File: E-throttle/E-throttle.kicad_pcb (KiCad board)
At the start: 2 copper layers, 100 x 100 mm, 62 parts, among them IC1 BTS441TG, J3 Conn_01x11, J4 Conn_01x11, J5 776087-1, J9 Micro_SD_Card, Q1 NMOS, SW1 SW_Push, U1 74HC123, U2 LM317_SOT-223, U3 LM317_SOT-223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

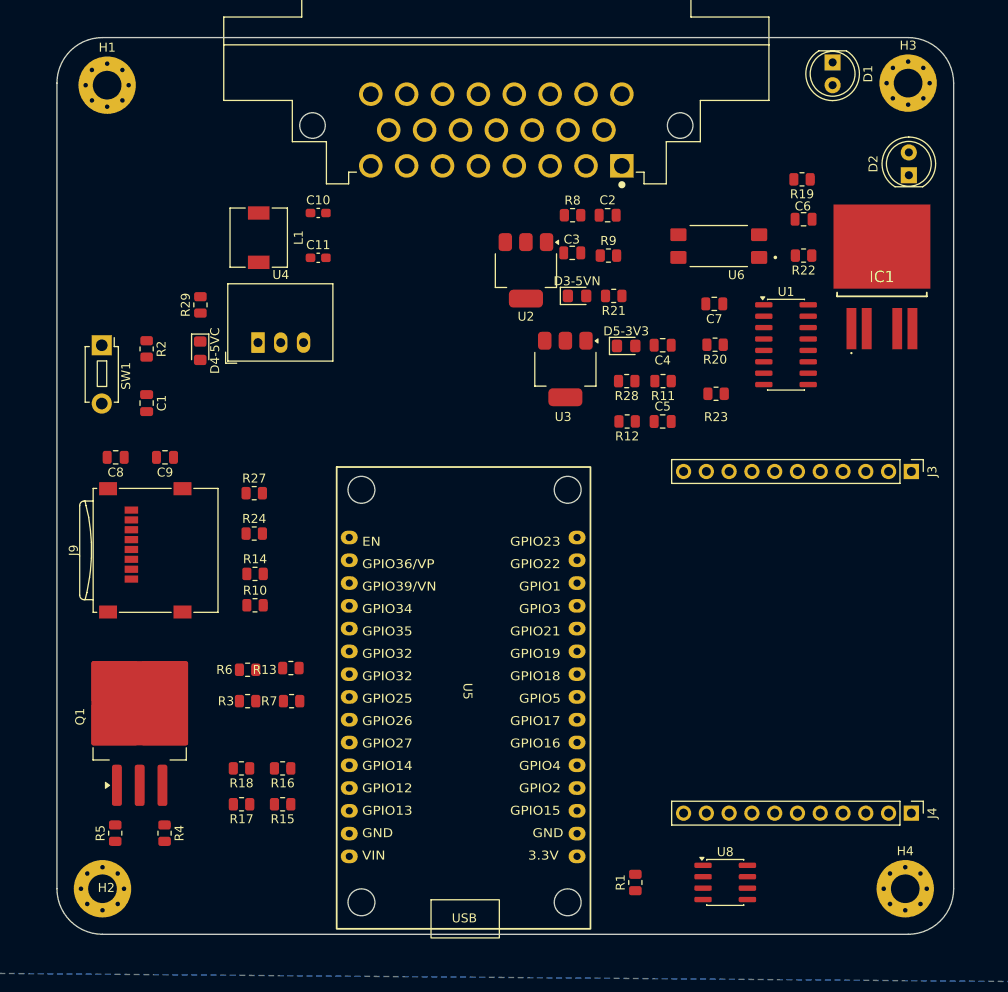
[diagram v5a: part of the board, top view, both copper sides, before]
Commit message: Added majority of routing to PCB layout
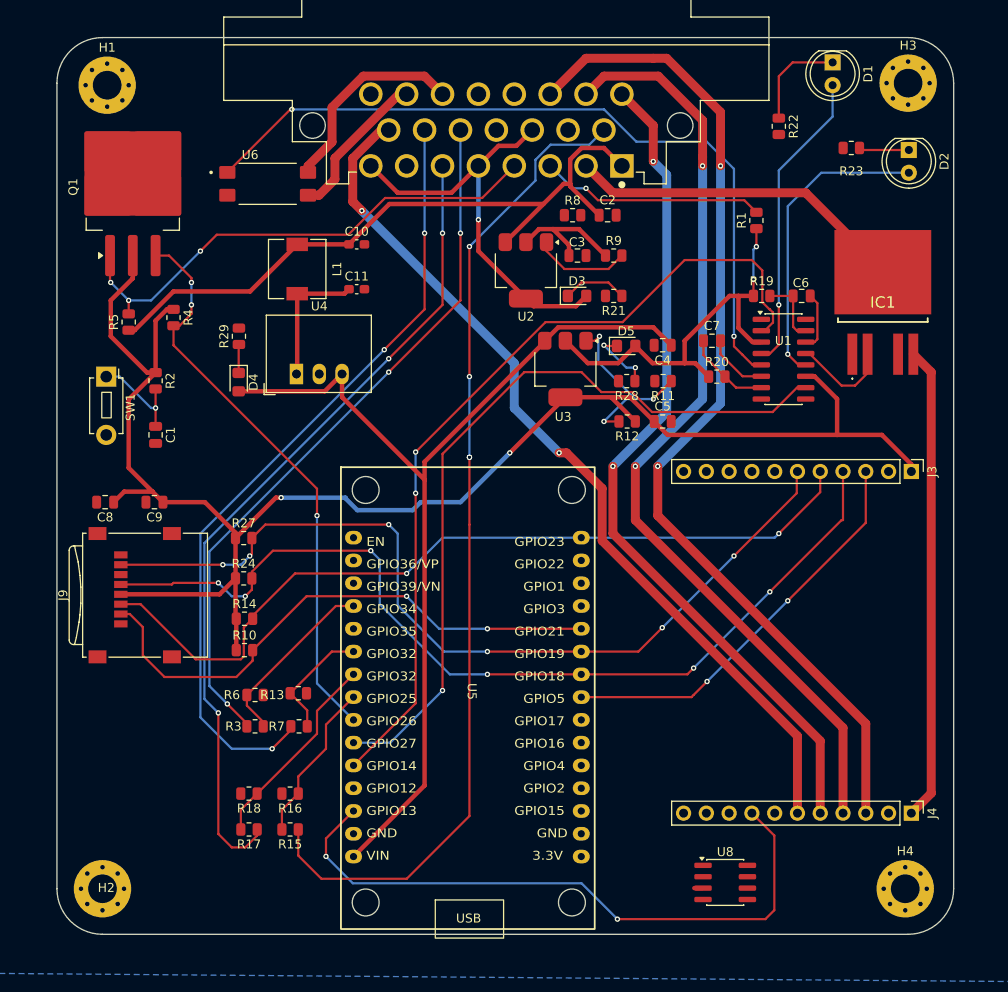
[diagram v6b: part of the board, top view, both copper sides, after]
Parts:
- moved R1 75.0 mm to (232.7, 53.9)
- moved Q1 59.1 mm to (163.2, 50.2)
- moved R4 57.5 mm to (167.7, 64.7)
- moved R5 57.0 mm to (162.7, 65.2)
- moved U6 50.8 mm to (178.2, 49.8), turned to 0 degrees
- moved R23 31.3 mm to (243.3, 45.8)
- moved R22 14.7 mm to (235.2, 43.4), turned to -90 degrees
- moved R19 13.8 mm to (233.3, 62.3), turned to 0 degrees
- moved C6 8.55 mm to (237.8, 62.3)
- moved C10 5.54 mm to (188.2, 56.6)
- moved C11 5.54 mm to (188.2, 61.6)
- moved D4 5.54 mm to (175.0, 71.9)
- moved U4 5.54 mm to (181.4, 71.0)
- moved L1 5.54 mm to (181.5, 59.3)
- moved R29 5.54 mm to (175.0, 66.8)
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- renumbered D3-5VN to D3, D4-5VC to D4, D5-3V3 to D5
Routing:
- net +3V3: track 0.00 -> 229.4 mm, vias 0 -> 4
- net /STEP-2-: track 0.00 -> 113.8 mm, vias 0 -> 2
- net /TPS-SIG2: track 0.00 -> 111.2 mm, vias 0 -> 4
- net +5V: track 0.00 -> 110.1 mm
- net /STEP-2+: track 0.00 -> 105.8 mm, vias 0 -> 2
- net /SPI-SCK: track 0.00 -> 105.7 mm, vias 0 -> 6
- net /STEP-1+: track 0.00 -> 99.4 mm, vias 0 -> 2
- net /SPI-MISO: track 0.00 -> 98.6 mm, vias 0 -> 6
- net /STEP-1-: track 0.00 -> 94.3 mm, vias 0 -> 2
- net /ESP_HEARTBEAT_L1: track 0.00 -> 93.9 mm, vias 0 -> 2
- net /SPI-MOSI: track 0.00 -> 92.6 mm, vias 0 -> 2
- net /TPS-SIG1: track 0.00 -> 92.3 mm, vias 0 -> 3
- net /APPS-SIG2: track 0.00 -> 88.7 mm, vias 0 -> 3
- net /ESP_HEARTBEAT_L2: track 0.00 -> 86.0 mm, vias 0 -> 1
- net /WD_ENABLE_STEP_RELAY: track 0.00 -> 85.9 mm, vias 0 -> 2
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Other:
- board text added: "GPIO19"

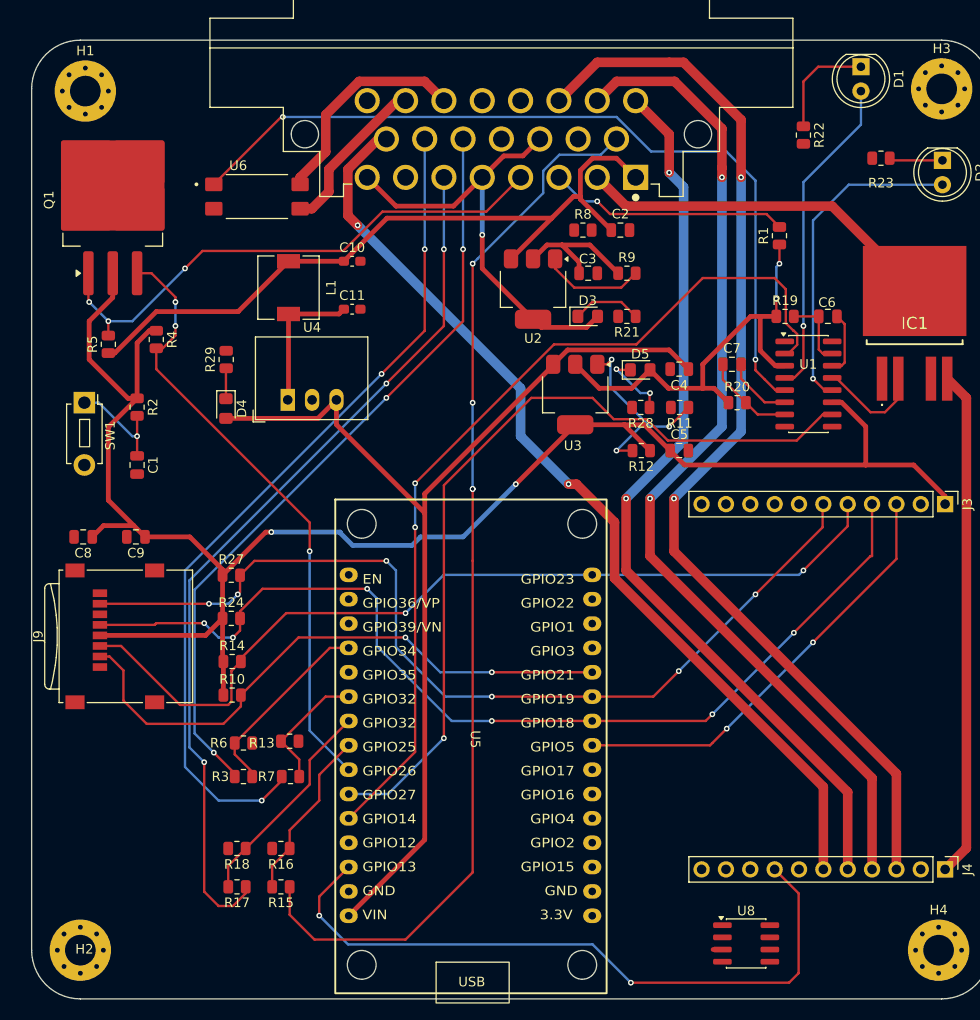
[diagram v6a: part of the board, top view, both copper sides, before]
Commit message: added a few ground vias
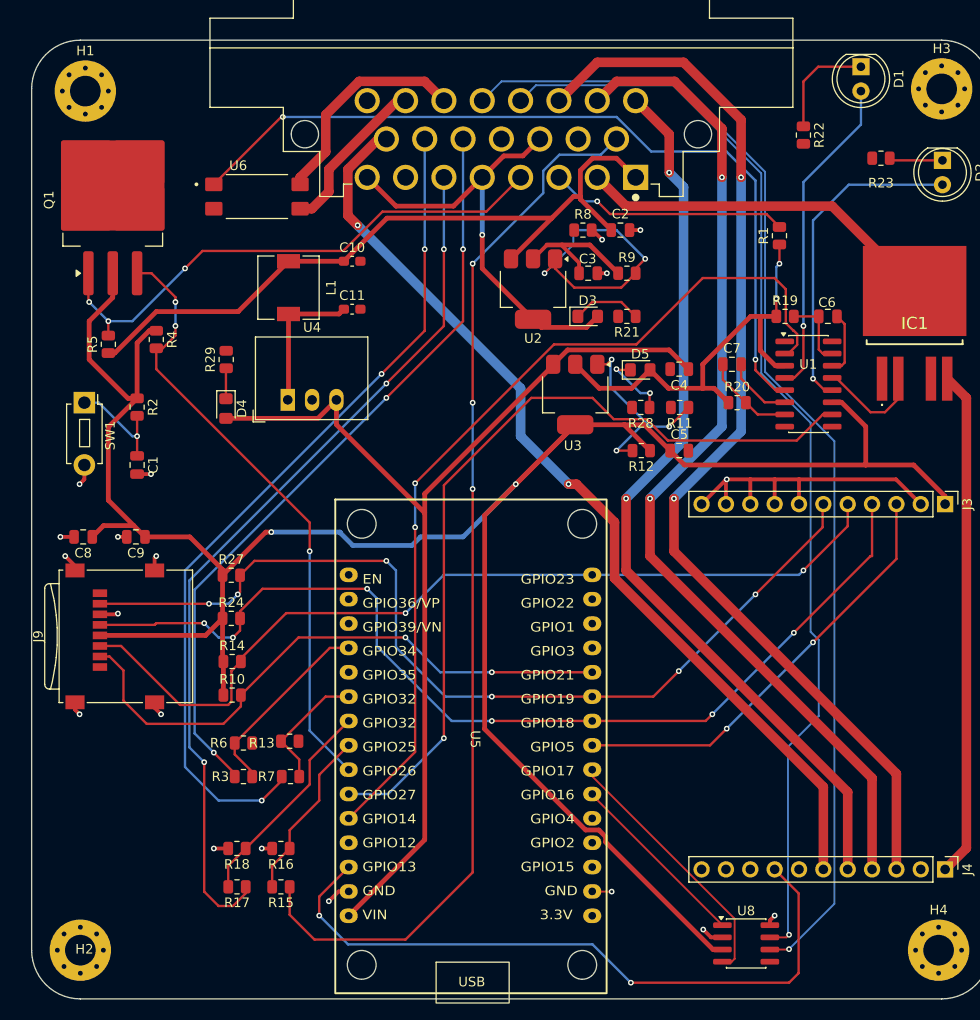
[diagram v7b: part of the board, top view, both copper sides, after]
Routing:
- net /CAN-L: track 0.00 -> 122.3 mm, vias 0 -> 1
- net /CAN-H: track 0.00 -> 115.0 mm, vias 0 -> 1
- net +3V3: track 229.4 -> 298.8 mm
- net GND: track 0.00 -> 61.9 mm, vias 0 -> 18
- net /CAN-RX: track 0.00 -> 27.3 mm
- net /CAN-TX: track 0.00 -> 19.3 mm
- net Net-(U2-ADJ): track 10.8 -> 29.2 mm, vias 0 -> 2
- net unconnected-(U5-GND-Pad17): track 0.00 -> 2.04 mm, vias 0 -> 1
- net +5V-SENSORS: track 61.1 -> 62.6 mm
- net /TPS-SIG2: vias 4 -> 3

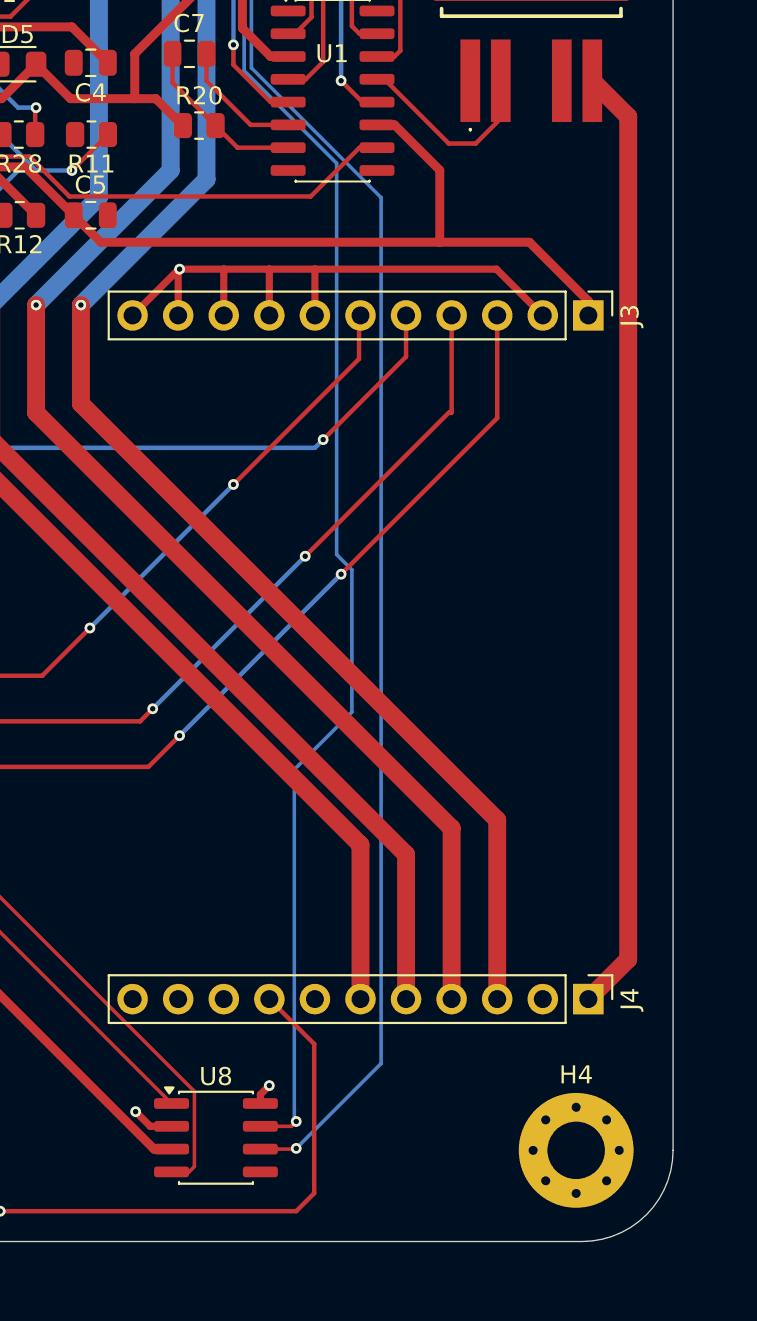
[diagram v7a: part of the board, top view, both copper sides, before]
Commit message: Fix Stepper Driver Spacing
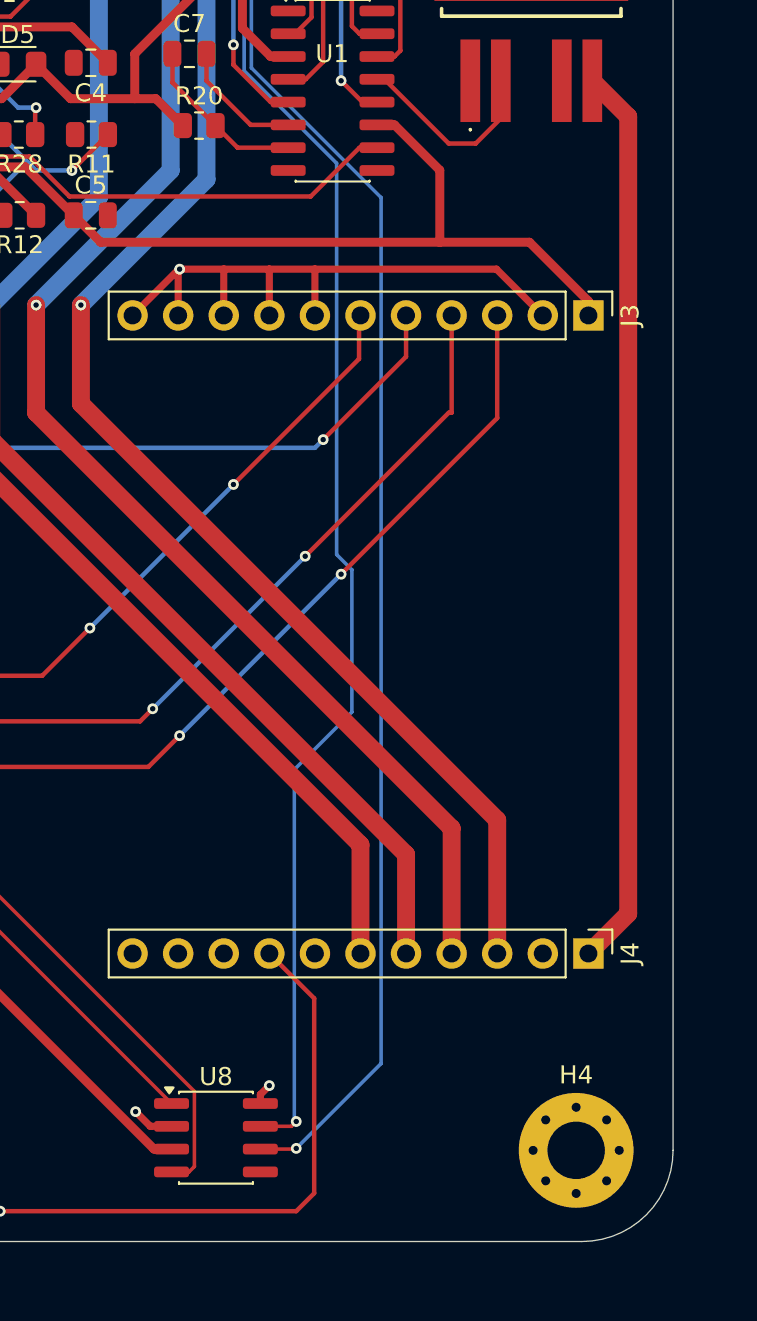
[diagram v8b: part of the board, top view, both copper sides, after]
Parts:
- moved J4 2.54 mm to (250.0, 117.5)
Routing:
- net /DIAG0: track 71.5 -> 74.0 mm
- net /STEP-2-: track 113.8 -> 111.3 mm
- net /STEP-1-: track 94.3 -> 91.8 mm
- net /STEP-1+: track 99.4 -> 96.8 mm
- net +12VStep-SAFE: track 52.9 -> 50.4 mm
- net /STEP-2+: track 105.8 -> 103.3 mm
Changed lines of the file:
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@@
 	(net 68 "Net-(D5-K)")
 	(footprint "Connector_PinHeader_2.54mm:PinHeader_1x11_P2.54mm_Vertical"
-		(locked yes)
 		(layer "F.Cu")
-		(at 250 120 -90)
+		(at 250 117.46 -90)
 		(descr "Through hole straight pin header, 1x11, 2.54mm pitch, single row")
 		(tags "Through hole pin header THT 1x11 2.54mm single row")
@@
 		(layer "Edge.Cuts")
 	)
-	(gr_line
-		(start 154.72 128.43)
-		(end 154.72 38.59)
+	(gr_arc
+		(start 249.64 33.51)
+		(mid 253.232102 34.997898)
+		(end 254.72 38.59)
 		(stroke
 			(width 0.05)
@@
 	)
 	(gr_line
-		(start 249.64 33.51)
-		(end 159.8 33.51)
+		(start 254.72 128.43)
+		(end 254.72 38.59)
 		(stroke
 			(width 0.05)
@@
 		(layer "Edge.Cuts")
 	)
-	(gr_arc
+	(gr_line
 		(start 249.64 33.51)
-		(mid 253.232102 34.997898)
-		(end 254.72 38.59)
+		(end 159.8 33.51)
 		(stroke
 			(width 0.05)
@@
 		(layer "Edge.Cuts")
 	)
-	(gr_line
-		(start 249.64 133.51)
-		(end 159.8 133.51)
+	(gr_arc
+		(start 254.72 128.43)
+		(mid 253.232102 132.022102)
+		(end 249.64 133.51)
 		(stroke
 			(width 0.05)
@@
 		(layer "Edge.Cuts")
 	)
-	(gr_arc
-		(start 254.72 128.43)
-		(mid 253.232102 132.022102)
-		(end 249.64 133.51)
+	(gr_line
+		(start 249.64 133.51)
+		(end 159.8 133.51)
 		(stroke
 			(width 0.05)
@@
 	)
 	(gr_line
-		(start 254.72 128.43)
-		(end 254.72 38.59)
+		(start 154.72 128.43)
+		(end 154.72 38.59)
 		(stroke
 			(width 0.05)
@@
 	)
 	(segment
-		(start 252.22 117.78)
-		(end 250 120)
+		(start 252.22 115.24)
+		(end 250 117.46)
 		(width 1)
 		(layer "F.Cu")
@@
 	(segment
 		(start 252.22 70.82)
-		(end 252.22 117.78)
+		(end 252.22 115.24)
 		(width 1)
 		(layer "F.Cu")
@@
 	)
 	(segment
-		(start 242.38 120)
-		(end 242.38 110.48)
-		(width 1)
-		(layer "F.Cu")
-		(net 21)
-	)
-	(segment
 		(start 215.7335 37.8065)
 		(end 221.783829 37.8065)
@@
 	)
 	(segment
+		(start 242.38 110.48)
+		(end 242.38 117.46)
+		(width 1)
+		(layer "F.Cu")
+		(net 21)
+	)
+	(segment
 		(start 219.22 87.32)
 		(end 219.22 81.32)
@@
 	)
 	(segment
-		(start 244.92 110.02)
-		(end 244.92 120)
+		(start 213.72 35.82)
+		(end 222.72 35.82)
 		(width 1)
 		(layer "F.Cu")
@@
 	)
 	(segment
-		(start 213.72 35.82)
-		(end 222.72 35.82)
+		(start 244.92 110.02)
+		(end 244.92 117.46)
 		(width 1)
 		(layer "F.Cu")
@@
 	)
 	(segment
-		(start 234.72 130.82)
-		(end 233.72 131.82)
+		(start 233.72 131.82)
+		(end 234.72 130.82)
 		(width 0.25)
 		(layer "F.Cu")
@@
 	)
 	(segment
-		(start 232.22 120)
-		(end 234.72 122.5)
+		(start 187.79246 119.759813)
+		(end 184.72 122.832273)
 		(width 0.25)
 		(layer "F.Cu")
@@
 	)
 	(segment
-		(start 217.22 131.82)
-		(end 233.72 131.82)
+		(start 234.72 130.82)
+		(end 234.72 119.96)
 		(width 0.25)
 		(layer "F.Cu")
@@
 	)
 	(segment
-		(start 187.79246 119.759813)
-		(end 184.72 122.832273)
+		(start 234.72 119.96)
+		(end 232.22 117.46)
 		(width 0.25)
 		(layer "F.Cu")
@@
 	)
 	(segment
-		(start 234.72 122.5)
-		(end 234.72 130.82)
+		(start 217.22 131.82)
+		(end 233.72 131.82)
 		(width 0.25)
 		(layer "F.Cu")
@@
 	)
 	(segment
-		(start 237.3 111.4)
-		(end 237.3 120)
+		(start 211.546949 79.82)
+		(end 215.519 83.792051)
 		(width 1)
 		(layer "F.Cu")
@@
 	)
 	(segment
-		(start 211.546949 79.82)
-		(end 215.519 83.792051)
+		(start 237.3 111.4)
+		(end 237.3 117.46)
 		(width 1)
 		(layer "F.Cu")
@@
 	)
 	(segment
-		(start 239.84 120)
-		(end 239.84 111.94)
+		(start 239.84 111.94)
+		(end 239.84 117.46)
 		(width 1)
 		(layer "F.Cu")
